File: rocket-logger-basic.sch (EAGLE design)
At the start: 63 parts, among them IC1 CC430F513X, U1 MAX1555, X1 0896BM15A0001, X2 USB-MICROB, X3 SMA-142-0701-801/806

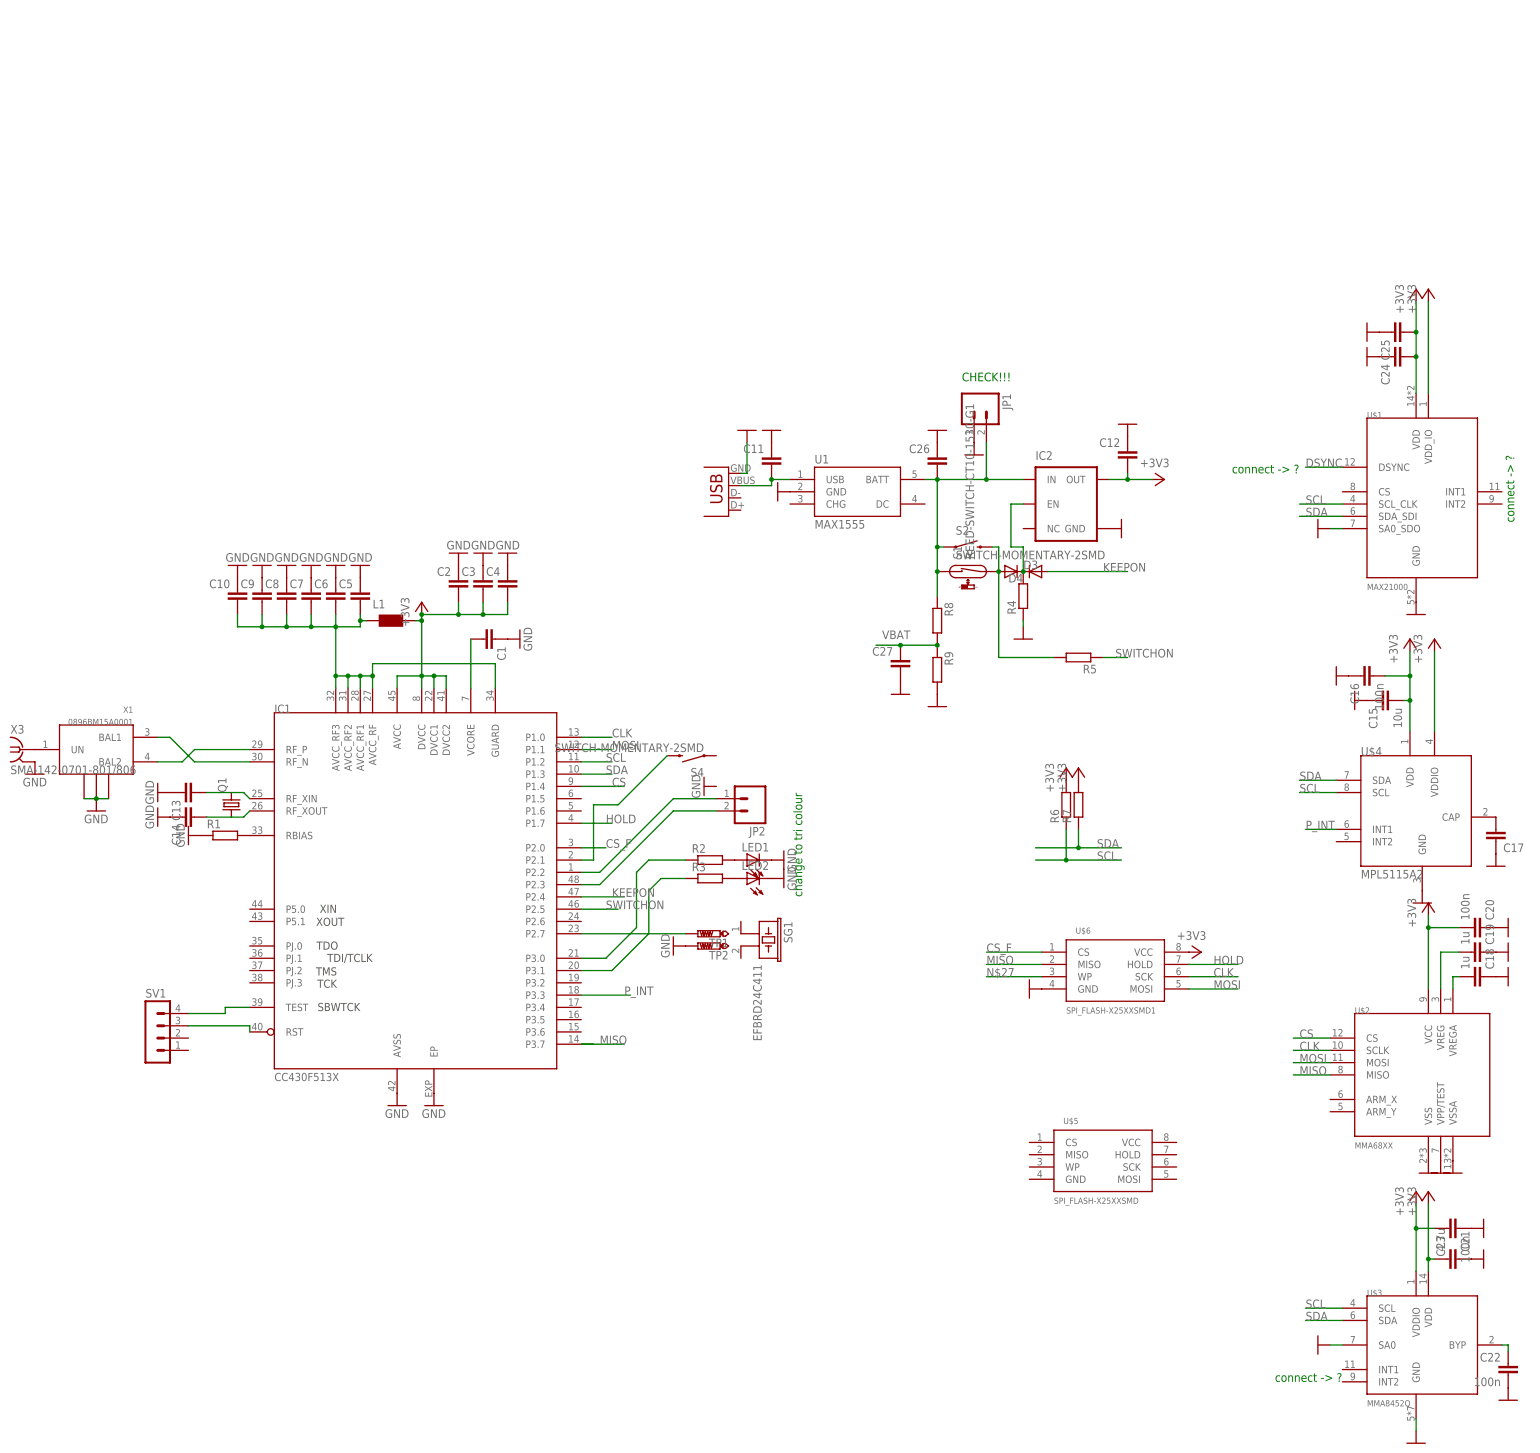
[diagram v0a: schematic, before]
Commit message: added mini logger
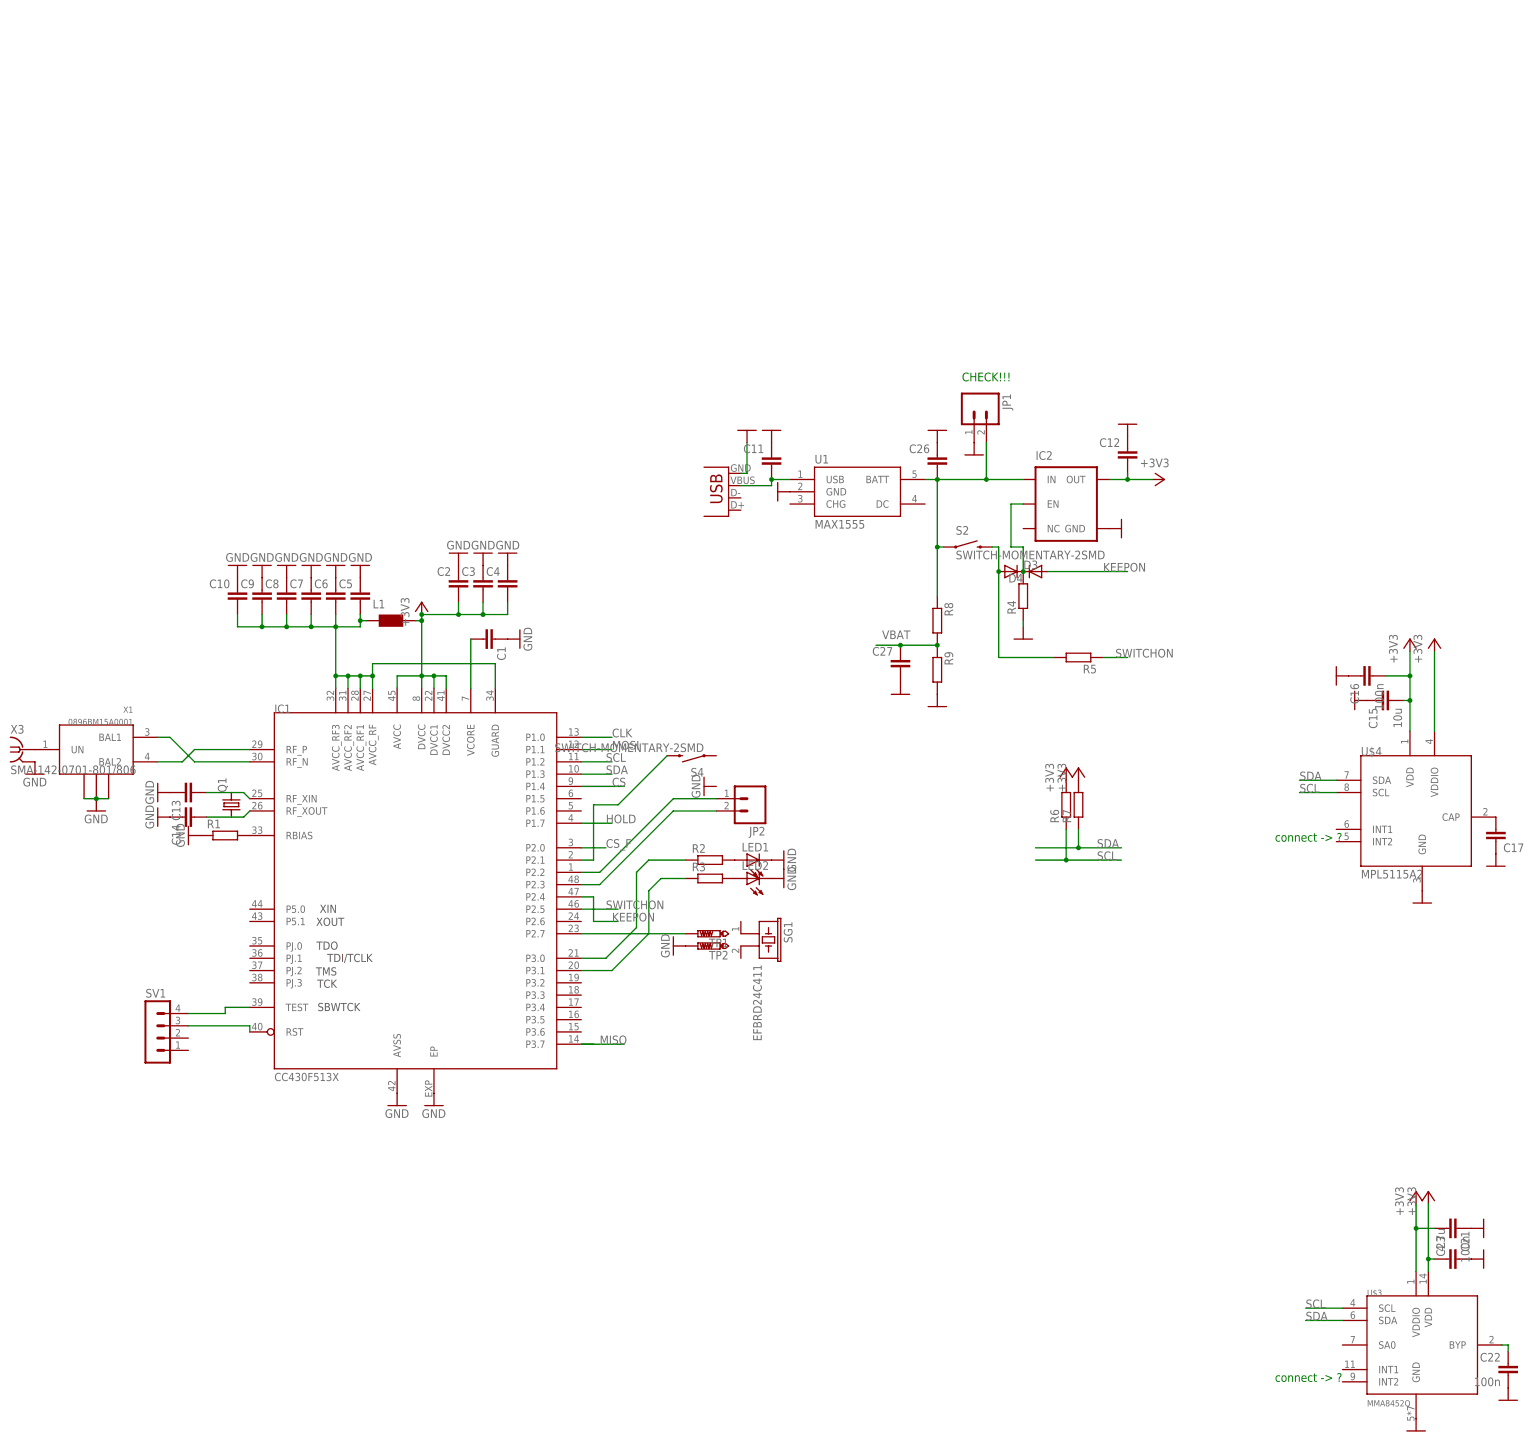
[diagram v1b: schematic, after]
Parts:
- removed C18, C19: 1u, resistor:C-EUC0402
- removed C20: 100n, resistor:C-EUC0402
- removed C24, C25: (no value), resistor:C-EUC0402
- removed S1: REED-SWITCH-CT10-1530-G1, switch-reed:REED-SWITCH-CT10-1530-G1
- removed U$1: MAX21000, Mine:MAX21000
- removed U$2: MMA68XX, Mine:MMA68XX
- removed U$5: SPI_FLASH-X25XXSMD, SparkFun:SPI_FLASH-X25XXSMD
- removed U$6: SPI_FLASH-X25XXSMD1, SparkFun:SPI_FLASH-X25XXSMD1
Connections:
- removed net DSYNC: U$1.DSYNC
- removed net N$14: C18.2, U$2.VREGA
- removed net N$15: C19.2, U$2.VREG
- removed net N$27: U$6.WP
- removed net P_INT: IC1.P3.3, U$4.INT1
- net +3V3: no longer C20.2, C24.2, C25.2, U$1.VDD, U$1.VDD_IO, U$2.VCC, U$6.VCC
- net CLK: no longer U$2.SCLK, U$6.SCK
- net CS: no longer U$2.CS
- net CS_F: no longer U$6.CS
- net GND: no longer C18.1, C19.1, C20.1, C24.1, C25.1, U$1.GND, U$1.SA0_SDO, U$2.VPP/TEST, U$2.VSS, U$2.VSSA, U$3.SA0, U$6.GND
- net HOLD: no longer U$6.HOLD
- net MISO: no longer U$2.MISO, U$6.MISO
- net MOSI: no longer U$2.MOSI, U$6.MOSI
- net N$2: no longer S1.1
- net N$24: no longer S1.2
- net SCL: no longer U$1.SCL_CLK
- net SDA: no longer U$1.SDA_SDI
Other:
- note removed: "change to tri colour"

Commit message: removed accel from simple verison, done some routing on main one
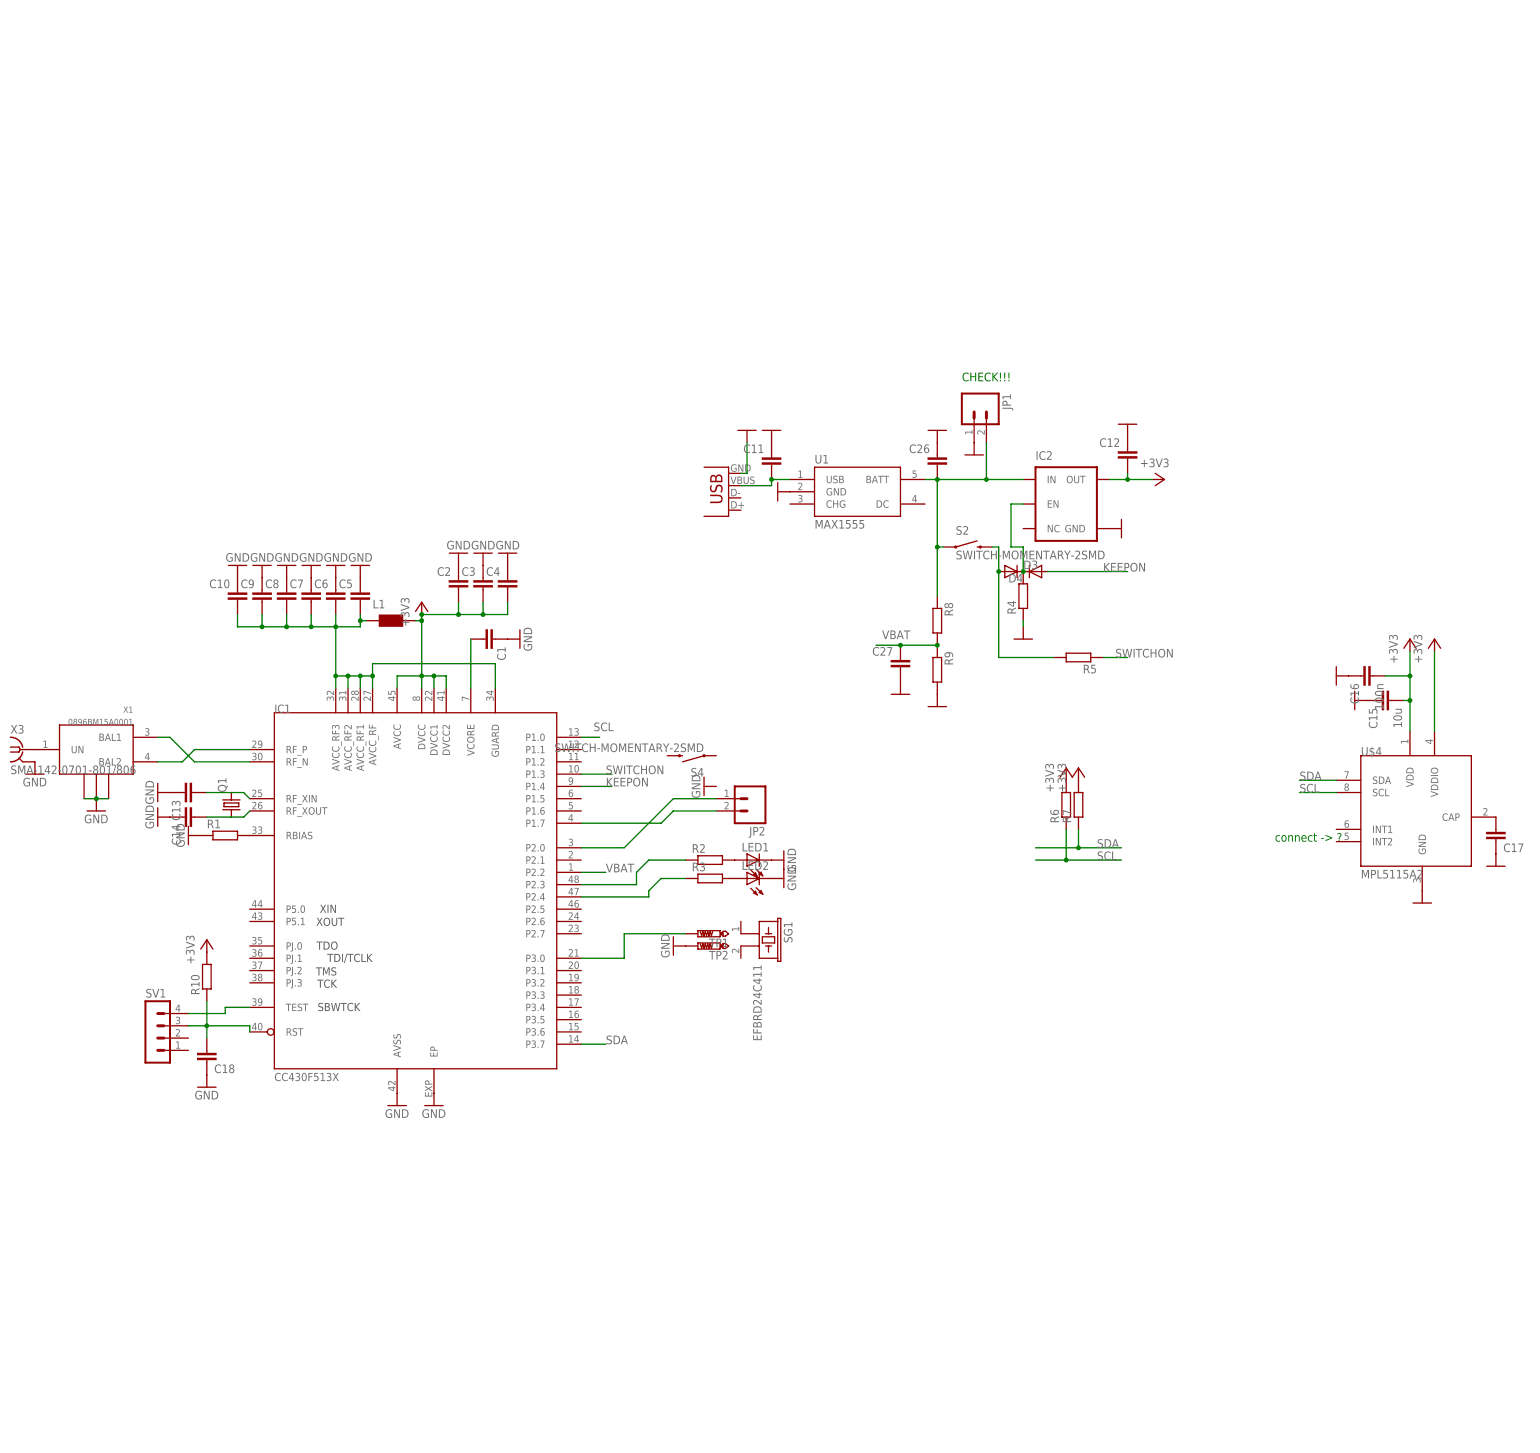
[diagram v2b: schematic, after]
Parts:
- removed C21: 4.7u, resistor:C-EUC0402
- removed C22, C23: 100n, resistor:C-EUC0402
- removed U$3: MMA8452Q, Mine:MMA8452Q
- added C18: (no value), resistor:C-EUC0402
- added R10: (no value), rcl:R-EU_R0402
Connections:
- removed net CLK: IC1.P1.0
- removed net CS: IC1.P1.4
- removed net CS_F: IC1.P2.0
- removed net HOLD: IC1.P1.7
- removed net MISO: IC1.P3.7
- removed net MOSI: IC1.P1.1
- removed net N$19: C22.1, U$3.BYP
- removed net N$28: IC1.P2.1, S4.2
- net +3V3: now also R10.2; no longer C21.2, C23.1, U$3.VDD, U$3.VDDIO
- net GND: now also C18.1; no longer C21.1, C22.2, C23.2, U$3.GND
- net KEEPON: now also IC1.P1.4; no longer IC1.P2.4
- net N$11: now also IC1.P2.0; no longer IC1.P2.2
- net N$12: now also IC1.P1.7; no longer IC1.P2.3
- net N$16: now also IC1.P2.3; no longer IC1.P3.0
- net N$17: now also IC1.P2.4; no longer IC1.P3.1
- net N$26: now also C18.2, R10.1
- net N$29: now also IC1.P3.0; no longer IC1.P2.7
- net SCL: now also IC1.P1.0; no longer IC1.P1.2, U$3.SCL
- net SDA: now also IC1.P3.7; no longer IC1.P1.3, U$3.SDA
- net SWITCHON: now also IC1.P1.3; no longer IC1.P2.5
- net VBAT: now also IC1.P2.2
